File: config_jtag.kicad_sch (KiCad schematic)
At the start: 12 parts, among them J1 Conn_01x06, SW1 SW_Push, U7 W25Q128JVS

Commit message: Add optional ESP32-C3 WiFi sheet, convert hand-solder parts to through-hole
- New wifi sheet: ESP32-C3-MINI-1 module on SPI to spare FPGA bank 34, with EN/boot-strap networks, 3V3 bypass/bulk caps and a UART debug header
- Replace SMD hand-solder resistors, LEDs, zener, fuse and ceramic caps with THT equivalents; bulk 10uF/22uF caps become polarized electrolytics
- Fill in LCSC part numbers for the new parts and regenerate BOM and ERC report
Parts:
- C85: footprint Capacitor_SMD:C_0603_1608Metric_Pad1.08x0.95mm_HandSolder -> Capacitor_THT:C_Disc_D3.0mm_W2.0mm_P2.50mm; LCSC Part (none) -> C5632430
- R18, R19, R20, R21, R22, R23, R24, R25: footprint Resistor_SMD:R_0603_1608Metric_Pad0.98x0.95mm_HandSolder -> Resistor_THT:R_Axial_DIN0207_L6.3mm_D2.5mm_P10.16mm_Horizontal
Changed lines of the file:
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@@
 			)
 		)
-		(property "Footprint" "Capacitor_SMD:C_0603_1608Metric_Pad1.08x0.95mm_HandSolder"
+		(property "Footprint" "Capacitor_THT:C_Disc_D3.0mm_W2.0mm_P2.50mm"
 			(at 87.3252 41.91 0)
 			(hide yes)
@@
 			)
 		)
+		(property "LCSC Part" "C5632430"
+			(at 0 0 0)
+			(hide yes)
+			(show_name no)
+			(do_not_autoplace no)
+			(effects
+				(font
+					(size 1.27 1.27)
+				)
+			)
+		)
 		(pin "2"
 		)
@@
 			)
 		)
-		(property "Footprint" "Resistor_SMD:R_0603_1608Metric_Pad0.98x0.95mm_HandSolder"
+		(property "Footprint" "Resistor_THT:R_Axial_DIN0207_L6.3mm_D2.5mm_P10.16mm_Horizontal"
 			(at 236.22 55.118 90)
 			(hide yes)
@@
 			)
 		)
-		(property "Footprint" "Resistor_SMD:R_0603_1608Metric_Pad0.98x0.95mm_HandSolder"
+		(property "Footprint" "Resistor_THT:R_Axial_DIN0207_L6.3mm_D2.5mm_P10.16mm_Horizontal"
 			(at 194.31 52.578 90)
 			(hide yes)
@@
 			)
 		)
-		(property "Footprint" "Resistor_SMD:R_0603_1608Metric_Pad0.98x0.95mm_HandSolder"
+		(property "Footprint" "Resistor_THT:R_Axial_DIN0207_L6.3mm_D2.5mm_P10.16mm_Horizontal"
 			(at 194.31 43.688 90)
 			(hide yes)
@@
 			)
 		)
-		(property "Footprint" "Resistor_SMD:R_0603_1608Metric_Pad0.98x0.95mm_HandSolder"
+		(property "Footprint" "Resistor_THT:R_Axial_DIN0207_L6.3mm_D2.5mm_P10.16mm_Horizontal"
 			(at 236.22 64.008 90)
 			(hide yes)
@@
 			)
 		)
-		(property "Footprint" "Resistor_SMD:R_0603_1608Metric_Pad0.98x0.95mm_HandSolder"
+		(property "Footprint" "Resistor_THT:R_Axial_DIN0207_L6.3mm_D2.5mm_P10.16mm_Horizontal"
 			(at 236.22 37.338 90)
 			(hide yes)
@@
 			)
 		)
-		(property "Footprint" "Resistor_SMD:R_0603_1608Metric_Pad0.98x0.95mm_HandSolder"
+		(property "Footprint" "Resistor_THT:R_Axial_DIN0207_L6.3mm_D2.5mm_P10.16mm_Horizontal"
 			(at 42.418 35.56 90)
 			(hide yes)
@@
 			)
 		)
-		(property "Footprint" "Resistor_SMD:R_0603_1608Metric_Pad0.98x0.95mm_HandSolder"
+		(property "Footprint" "Resistor_THT:R_Axial_DIN0207_L6.3mm_D2.5mm_P10.16mm_Horizontal"
 			(at 194.31 36.068 90)
 			(hide yes)
@@
 			)
 		)
-		(property "Footprint" "Resistor_SMD:R_0603_1608Metric_Pad0.98x0.95mm_HandSolder"
+		(property "Footprint" "Resistor_THT:R_Axial_DIN0207_L6.3mm_D2.5mm_P10.16mm_Horizontal"
 			(at 236.22 46.228 90)
 			(hide yes)

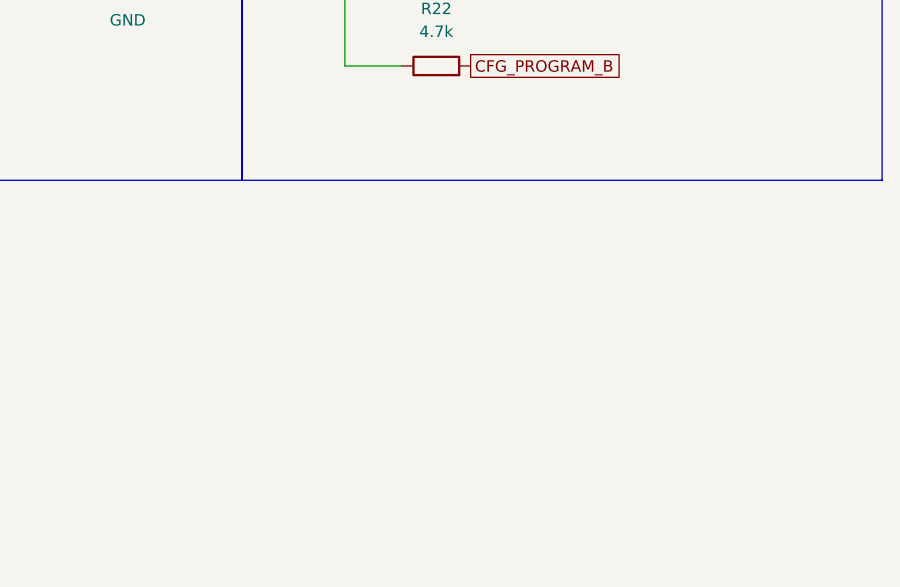
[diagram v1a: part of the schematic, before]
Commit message: Routing in progress: In3 power pours, DONE LED, DRC cleanup
- Add CFG_DONE 330R pull-up (R52) and DONE LED (D7, R53) per UG470
- Redraw In3.Cu pours to sit under their U6 balls (1V0 core, 1V8 strip,
  MGTAVCC, MGTAVTT); trim 5V_LC strip to y=50; zone clearance 0.2mm
- Remove 3V3/5V_LC traces from In4.Cu GND plane
- Custom rules: U6 BGA escape, solid GND on regulators/tight caps,
  1-spoke thermals on J4 and C22
- Fix clearance violations, remove dangling vias and stubs
- Remaining: GND pours split on In1.Cu/B.Cu by signal traces on In1.Cu
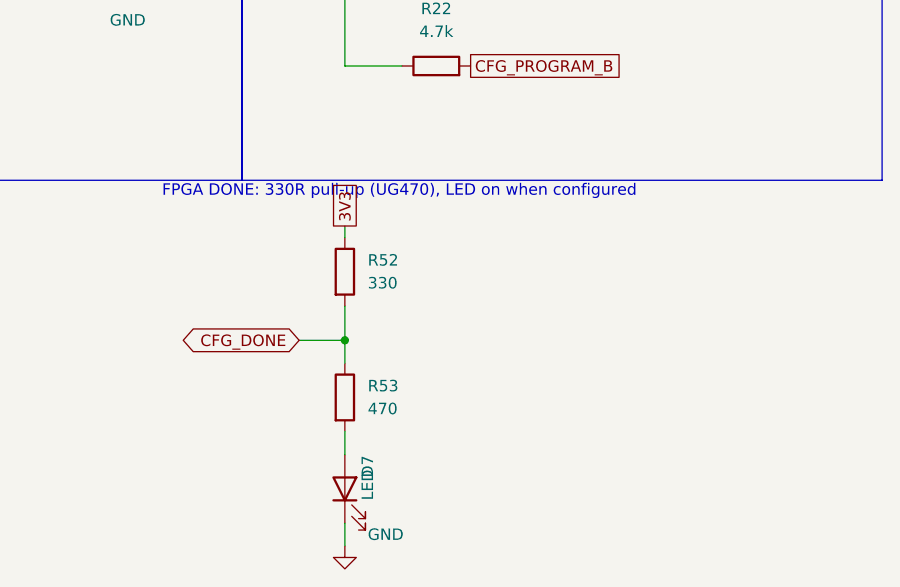
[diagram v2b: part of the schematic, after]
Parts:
- added D7: LED, LED_THT:LED_D3.0mm, symbol Device:LED
- added R52: 330, Resistor_THT:R_Axial_DIN0207_L6.3mm_D2.5mm_P10.16mm_Horizontal, symbol Device:R
- added R53: 470, Resistor_THT:R_Axial_DIN0207_L6.3mm_D2.5mm_P10.16mm_Horizontal, symbol Device:R
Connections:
- net 3V3: now also R52.1
- net GND: now also D7.1 (K)
- new net: D7.2 (A), R53.2
- new net CFG_DONE: R52.2, R53.1
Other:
- note added: "FPGA DONE: 330R pull-up (UG470), LED on when configured"
